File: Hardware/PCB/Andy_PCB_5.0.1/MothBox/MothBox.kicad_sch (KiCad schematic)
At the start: 0 parts

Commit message: updated photo LEDs and the power page
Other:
- sheet Photo LED's: file Photo LEDS's.kicad_sch -> Photo_LEDs.kicad_sch
- sheet UV LED PCB: file UV LED PCB.kicad_sch -> UV_LED_PCB.kicad_sch
- company: (none) -> Digital Naturalism Laboritories
- title: (none) -> MothBox
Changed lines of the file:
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@@
 	(generator_version "9.0")
 	(paper "A4")
+	(title_block
+		(title "MothBox")
+		(date "2025-07-12")
+		(rev "5.0.1")
+		(company "Digital Naturalism Laboritories")
+	)
 	(sheet
 		(at 176.53 45.72)
@@
 			)
 		)
-		(property "Sheetfile" "UV LED PCB.kicad_sch"
+		(property "Sheetfile" "UV_LED_PCB.kicad_sch"
 			(at 161.29 134.5696 0)
 			(effects
@@
 			)
 		)
-		(property "Sheetfile" "Photo LEDS's.kicad_sch"
+		(property "Sheetfile" "Photo_LEDs.kicad_sch"
 			(at 114.3 134.5696 0)
 			(effects

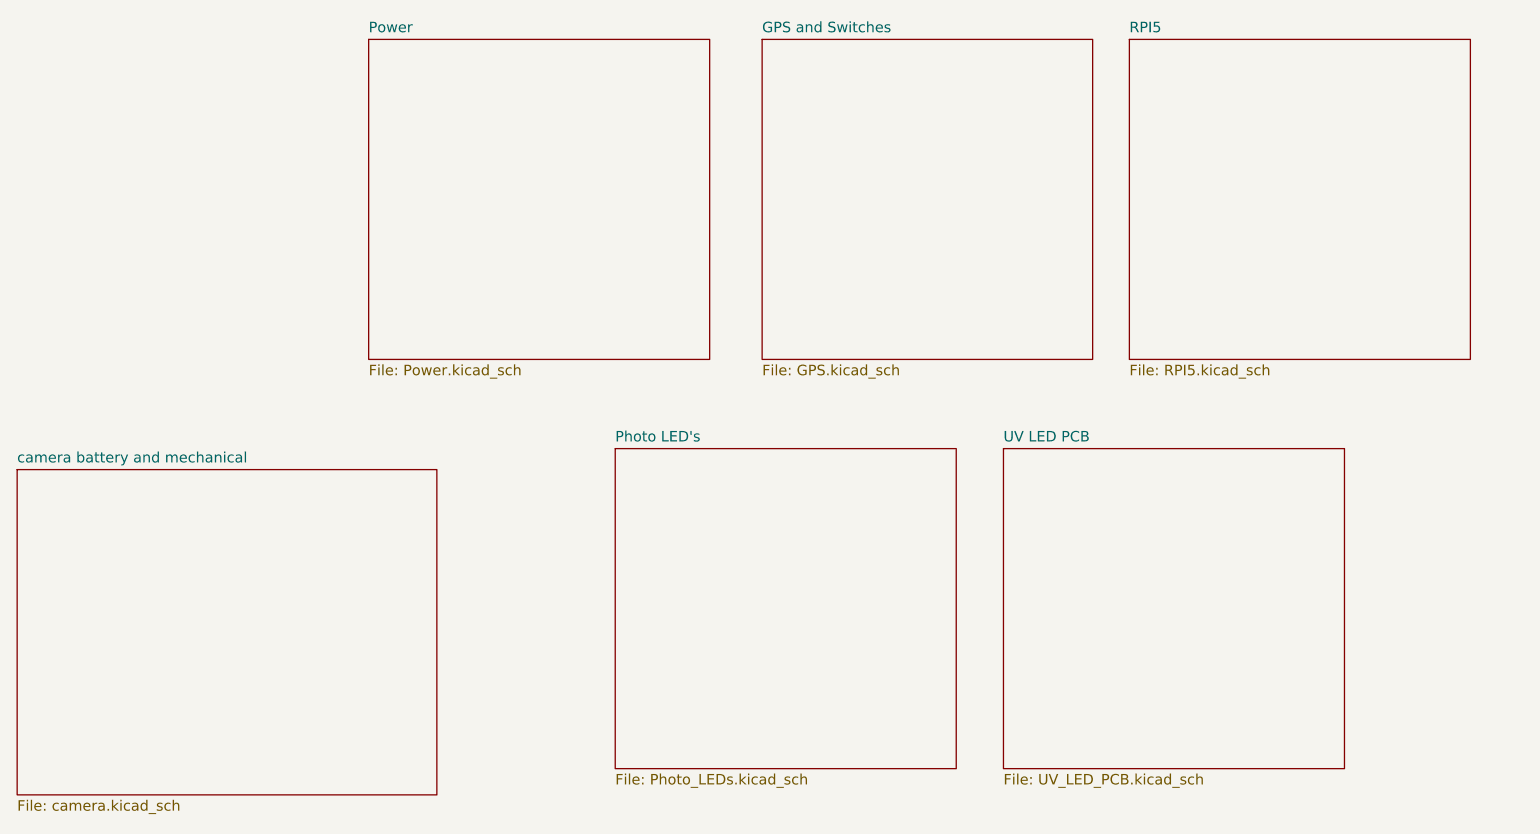
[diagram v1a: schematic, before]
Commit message: updated footprints and schematic
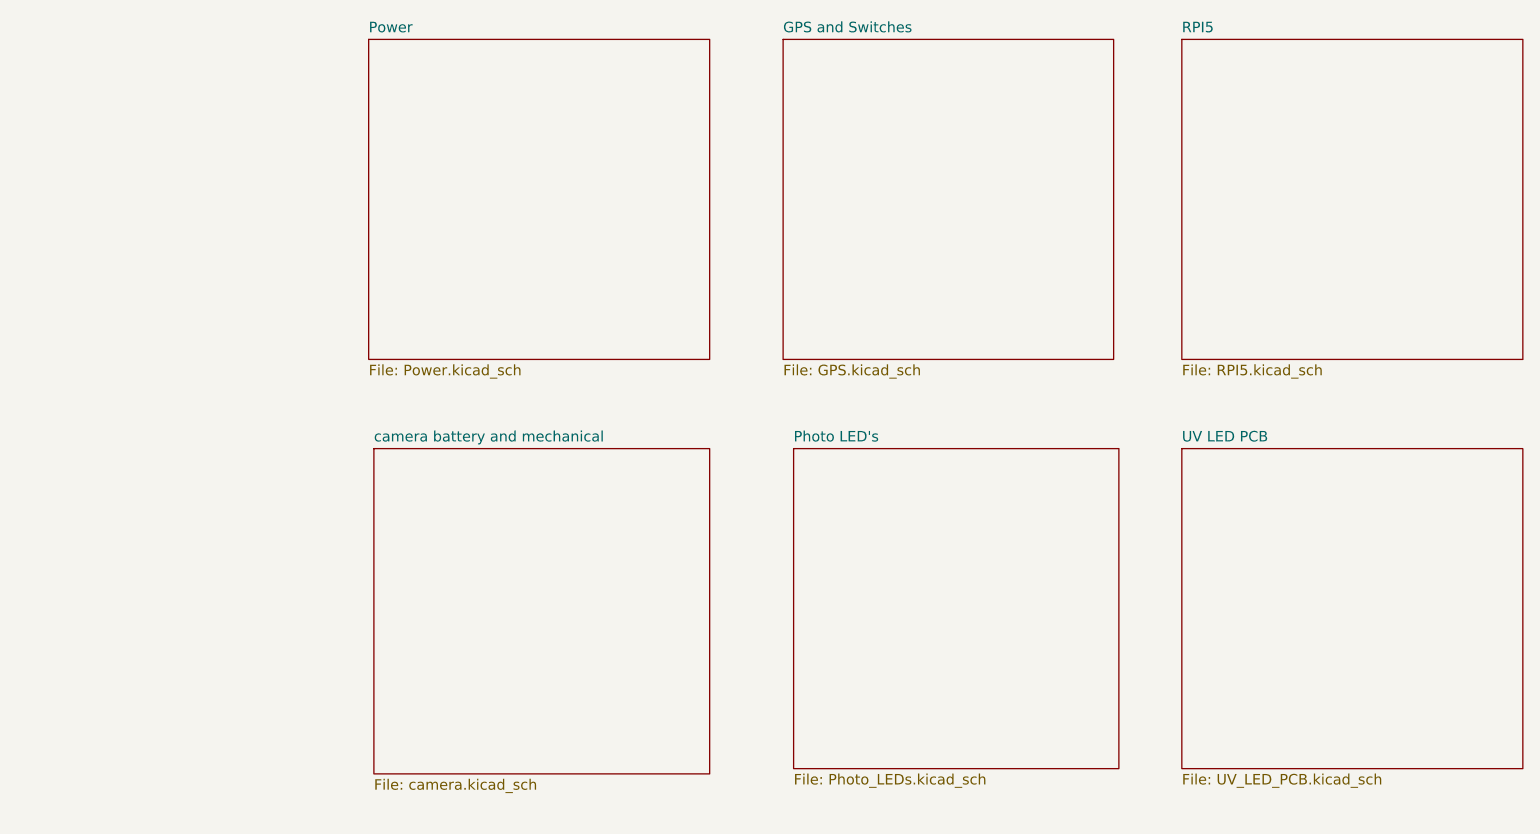
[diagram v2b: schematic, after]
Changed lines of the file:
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@@
 	)
 	(sheet
-		(at 176.53 45.72)
+		(at 182.88 45.72)
 		(size 41.275 38.735)
 		(exclude_from_sim no)
@@
 		)
 		(property "Sheetname" "RPI5"
-			(at 176.53 45.0084 0)
+			(at 182.88 45.0084 0)
 			(effects
 				(font
@@
 		)
 		(property "Sheetfile" "RPI5.kicad_sch"
-			(at 176.53 85.0396 0)
+			(at 182.88 85.0396 0)
 			(effects
 				(font
@@
 	)
 	(sheet
-		(at 161.29 95.25)
+		(at 182.88 95.25)
 		(size 41.275 38.735)
 		(exclude_from_sim no)
@@
 		)
 		(property "Sheetname" "UV LED PCB"
-			(at 161.29 94.5384 0)
+			(at 182.88 94.5384 0)
 			(effects
 				(font
@@
 		)
 		(property "Sheetfile" "UV_LED_PCB.kicad_sch"
-			(at 161.29 134.5696 0)
+			(at 182.88 134.5696 0)
 			(effects
 				(font
@@
 	)
 	(sheet
-		(at 41.91 97.79)
-		(size 50.8 39.37)
+		(at 85.09 95.25)
+		(size 40.64 39.37)
 		(exclude_from_sim no)
 		(in_bom yes)
@@
 		)
 		(property "Sheetname" "camera battery and mechanical"
-			(at 41.91 97.0784 0)
+			(at 85.09 94.5384 0)
 			(effects
 				(font
@@
 		)
 		(property "Sheetfile" "camera.kicad_sch"
-			(at 41.91 137.7446 0)
+			(at 85.09 135.2046 0)
 			(effects
 				(font
@@
 	)
 	(sheet
-		(at 132.08 45.72)
+		(at 134.62 45.72)
 		(size 40.005 38.735)
 		(exclude_from_sim no)
@@
 		)
 		(property "Sheetname" "GPS and Switches"
-			(at 132.08 45.0084 0)
+			(at 134.62 45.0084 0)
 			(effects
 				(font
@@
 		)
 		(property "Sheetfile" "GPS.kicad_sch"
-			(at 132.08 85.0396 0)
+			(at 134.62 85.0396 0)
 			(effects
 				(font
@@
 	)
 	(sheet
-		(at 114.3 95.25)
-		(size 41.275 38.735)
+		(at 135.89 95.25)
+		(size 39.37 38.735)
 		(exclude_from_sim no)
 		(in_bom yes)
@@
 		)
 		(property "Sheetname" "Photo LED's"
-			(at 114.3 94.5384 0)
+			(at 135.89 94.5384 0)
 			(effects
 				(font
@@
 		)
 		(property "Sheetfile" "Photo_LEDs.kicad_sch"
-			(at 114.3 134.5696 0)
-			(effects
-				(font
+			(at 135.89 134.5696 0)
+			(effects
+				(font

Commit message: before trimming top of PCB
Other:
- sheet GPS and Switches renamed GPS and Switches and Light Sensor
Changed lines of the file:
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@@
 			(color 0 0 0 0.0000)
 		)
-		(property "Sheetname" "GPS and Switches"
+		(property "Sheetname" "GPS and Switches and Light Sensor"
 			(at 134.62 45.0084 0)
 			(effects
